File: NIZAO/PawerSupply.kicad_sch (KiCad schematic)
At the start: 16 parts, among them U4 AP63203WU

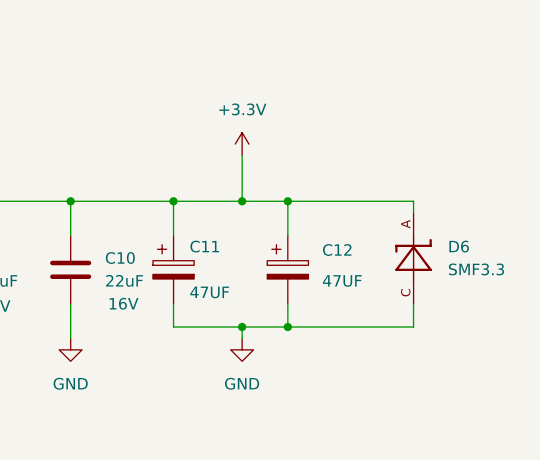
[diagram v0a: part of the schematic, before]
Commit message: Colocandos los 3d de los componetes en la placa NIZAO
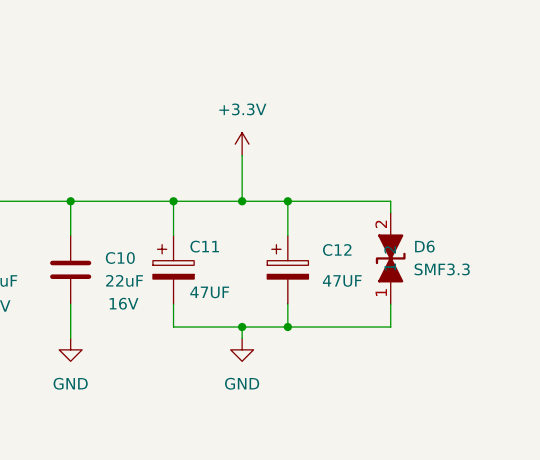
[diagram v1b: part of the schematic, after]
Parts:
- D6: footprint SMF3.3_SODFL3718X108N:SMF3.3_SODFL3718X108N -> JLCImport:SMF3_3CA_C6165153; symbol Snapeda:SMF3.3 -> JLCImport:SMF3_3CA_C6165153; LCSC (none) -> C6165153; Manufacturer (none) -> BORN; Manufacturer Part (none) -> SMF3.3CA
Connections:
- net +3.3V: now also D6.2; no longer D6.A
- net GND: now also D6.1; no longer D6.C
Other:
- moved on the sheet: D6
